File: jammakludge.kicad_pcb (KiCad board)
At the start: 2 copper layers, 55 parts, among them J1 Conn_02x28_Odd_Even, J2 Conn_02x28, J3 Conn_02x28

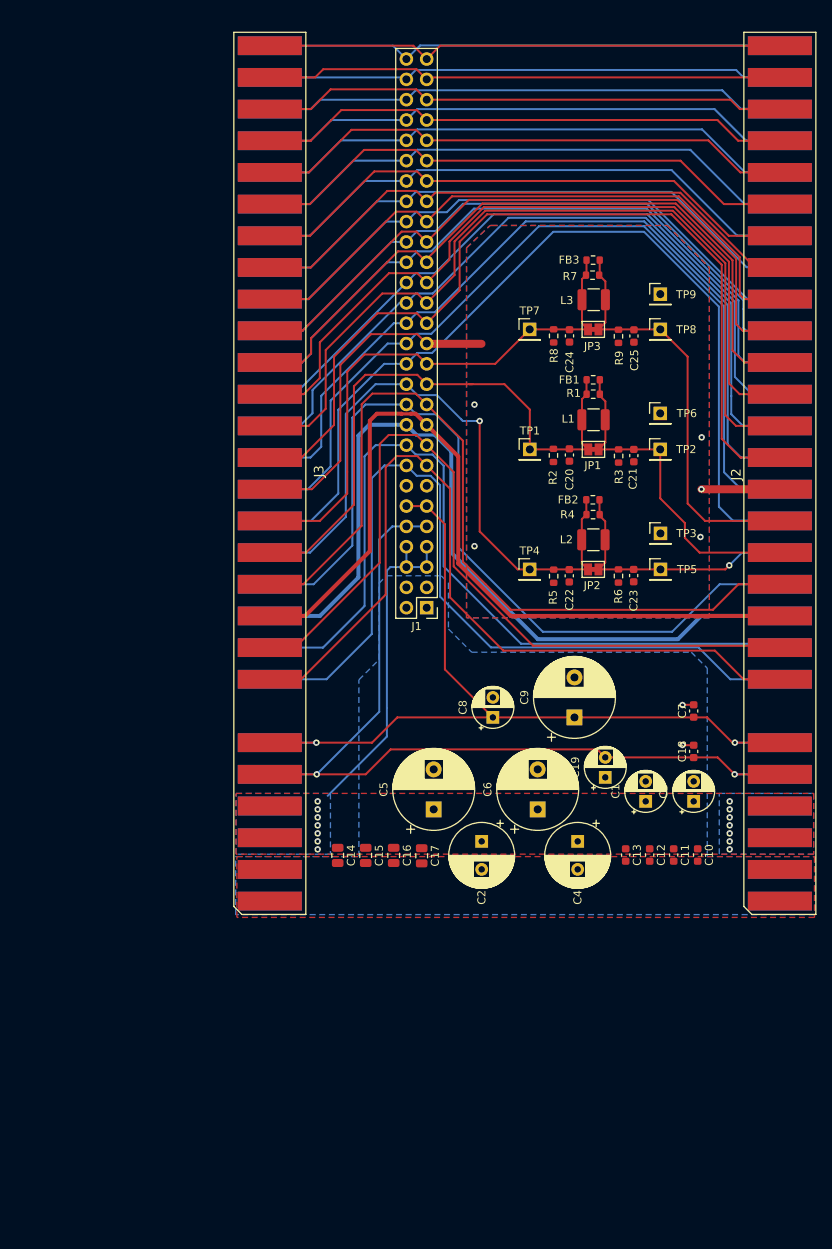
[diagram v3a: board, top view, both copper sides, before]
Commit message: Layout is basically complete, missing outline until dimensions can be double checked. DRC violations minimised but footprints (solder jumper and jamma edge connector) cause violations.
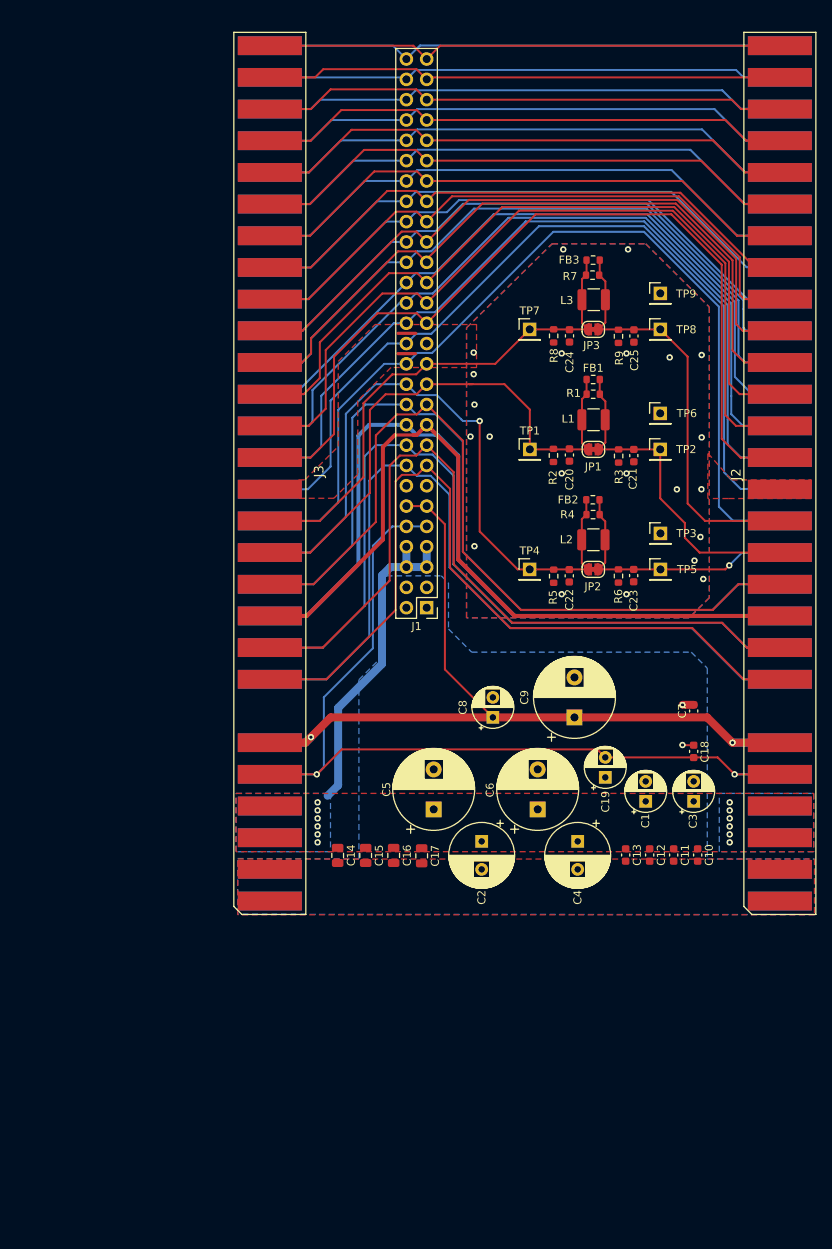
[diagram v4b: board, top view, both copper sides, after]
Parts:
- JP1, JP2, JP3: footprint Jumper:SolderJumper-2_P1.3mm_Bridged_Pad1.0x1.5mm -> Jumper:SolderJumper-2_P1.3mm_Bridged_RoundedPad1.0x1.5mm
- moved TP9 0.09 mm to (100.8, 79.0)
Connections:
- FB1 pad 1: (no net) -> /VidRedIn
- FB1 pad 2: (no net) -> /VidRed
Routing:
- net /VidGnd: track 52.3 -> 4.55 mm, vias 5 -> 22
- net /VidBlueIn: track 72.3 -> 67.9 mm
- net /Audio_+: track 103.9 -> 99.5 mm
- net /Speaker_+: track 102.1 -> 97.9 mm
- net /VidRedIn: track 74.0 -> 70.4 mm
- net /Speaker_-: track 103.7 -> 100.6 mm
- net /Meter_1: track 104.2 -> 101.1 mm
- net /Test_switch: track 111.3 -> 108.4 mm
- net /Meter_2: track 105.5 -> 102.6 mm
- net /Coin_1: track 104.9 -> 102.4 mm
- net /Audio_gnd: track 104.7 -> 102.5 mm
- net /Lockout_1: track 101.4 -> 99.9 mm
- net /P1_start: track 97.0 -> 95.6 mm
- net /Lockout_2: track 103.0 -> 102.2 mm
- net /VidSync: track 114.5 -> 115.1 mm
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
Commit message: added outline
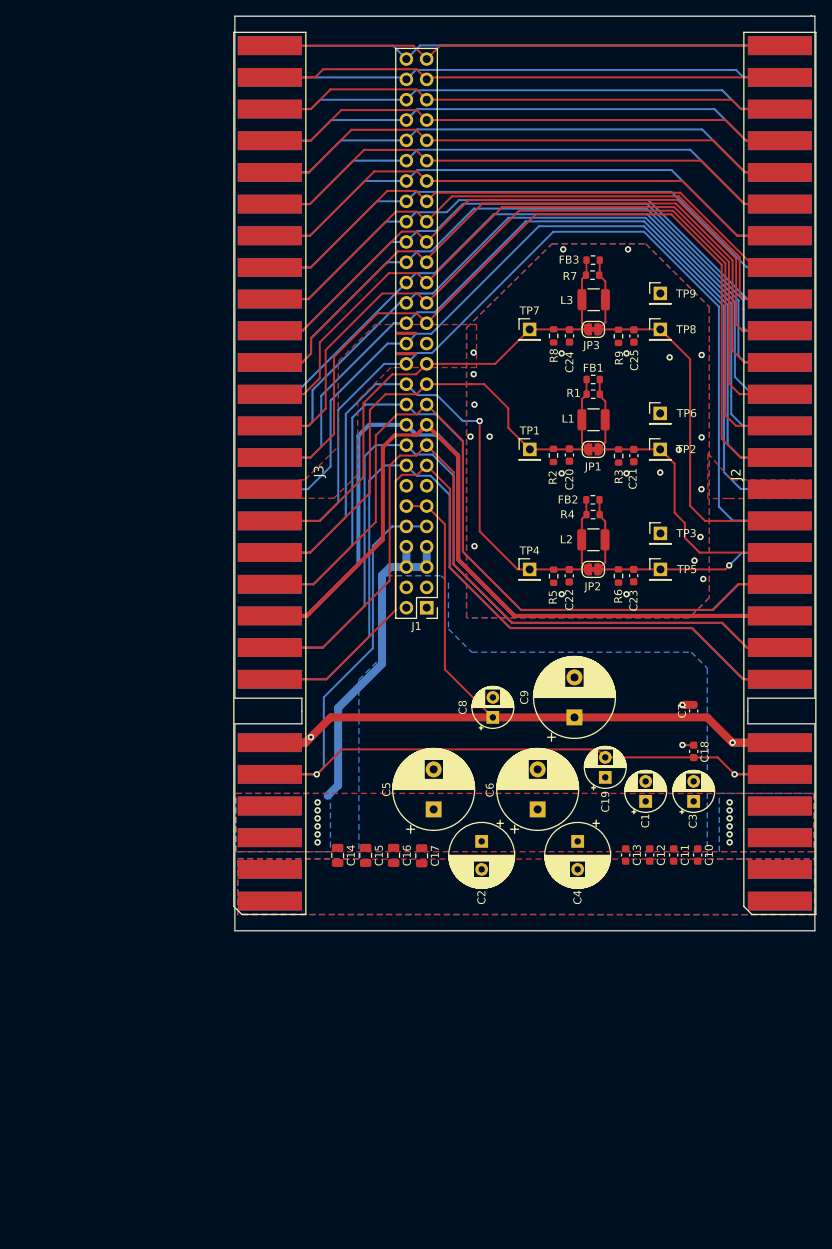
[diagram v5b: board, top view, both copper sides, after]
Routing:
- net /VidRedIn: track 70.4 -> 68.9 mm
- net /VidGnd: vias 22 -> 23
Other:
- board outline added: 72.5 x 114.3 mm
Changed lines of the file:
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@@
     )
   )
-  (segment (start 84.5196 93.5196) (end 81.3478 90.3478) (width 0.25) (layer "F.Cu") (net 1))
+  (gr_line (start 119.78 44.35) (end 119.6 44.35) (layer "Edge.Cuts") (width 0.05))
+  (gr_line (start 120.15 158.67) (end 47.65 158.67) (layer "Edge.Cuts") (width 0.05))
+  (gr_line (start 111.77 131.2) (end 111.77 129.6) (layer "Edge.Cuts") (width 0.05))
+  (gr_line (start 111.77 132.8) (end 120.15 132.8) (layer "Edge.Cuts") (width 0.05))
+  (gr_line (start 56.03 129.6) (end 47.65 129.6) (layer "Edge.Cuts") (width 0.05))
+  (gr_line (start 56.03 129.6) (end 56.03 131.2) (layer "Edge.Cuts") (width 0.05))
+  (gr_line (start 56.03 131.2) (end 56.03 132.8) (layer "Edge.Cuts") (width 0.05))
+  (gr_line (start 47.65 44.35) (end 120.15 44.35) (layer "Edge.Cuts") (width 0.05))
+  (gr_line (start 47.65 129.6) (end 47.65 44.35) (layer "Edge.Cuts") (width 0.05))
+  (gr_line (start 47.65 158.67) (end 47.65 132.8) (layer "Edge.Cuts") (width 0.05))
+  (gr_line (start 120.15 132.8) (end 120.15 158.67) (layer "Edge.Cuts") (width 0.05))
+  (gr_line (start 111.77 129.6) (end 120.15 129.6) (layer "Edge.Cuts") (width 0.05))
+  (gr_line (start 56.03 132.8) (end 47.65 132.8) (layer "Edge.Cuts") (width 0.05))
+  (gr_line (start 120.15 44.35) (end 120.15 129.6) (layer "Edge.Cuts") (width 0.05))
+  (gr_line (start 111.77 132.8) (end 111.77 131.2) (layer "Edge.Cuts") (width 0.05))
   (segment (start 52.0192 111.3972) (end 57.0728 111.3972) (width 0.25) (layer "F.Cu") (net 1))
   (segment (start 66.48 91.61) (end 70.3658 91.61) (width 0.25) (layer "F.Cu") (net 1))
@@
   (segment (start 57.0728 111.3972) (end 64.53 103.94) (width 0.25) (layer "F.Cu") (net 1))
   (segment (start 77.3478 90.3478) (end 76.9478 90.3478) (width 0.25) (layer "F.Cu") (net 1))
+  (segment (start 78.8078 90.3478) (end 76.9478 90.3478) (width 0.25) (layer "F.Cu") (net 1))
   (segment (start 91.6044 89.8386) (end 91.6044 91.6524) (width 0.25) (layer "F.Cu") (net 1))
   (segment (start 91.0385 94.7916) (end 91.0385 92.2183) (width 0.25) (layer "F.Cu") (net 1))
   (segment (start 91.0385 97.7383) (end 91.0385 94.7916) (width 0.25) (layer "F.Cu") (net 1))
   (segment (start 91.0385 92.2183) (end 91.5386 91.7182) (width 0.25) (layer "F.Cu") (net 1))
+  (segment (start 84.5196 98.5) (end 81.83 95.8104) (width 0.25) (layer "F.Cu") (net 1))
   (segment (start 64.53 93.56) (end 66.48 91.61) (width 0.25) (layer "F.Cu") (net 1))
   (segment (start 64.53 103.94) (end 64.53 93.56) (width 0.25) (layer "F.Cu") (net 1))
   (segment (start 76.9478 90.3478) (end 71.628 90.3478) (width 0.25) (layer "F.Cu") (net 1))
   (segment (start 91.8002 98.5) (end 91.0385 97.7383) (width 0.25) (layer "F.Cu") (net 1))
-  (segment (start 81.3478 90.3478) (end 76.9478 90.3478) (width 0.25) (layer "F.Cu") (net 1))
-  (segment (start 84.5196 98.5) (end 84.5196 93.5196) (width 0.25) (layer "F.Cu") (net 1))
+  (segment (start 81.83 95.8104) (end 81.83 93.37) (width 0.25) (layer "F.Cu") (net 1))
   (segment (start 70.3658 91.61) (end 71.628 90.3478) (width 0.25) (layer "F.Cu") (net 1))
+  (segment (start 81.83 93.37) (end 78.8078 90.3478) (width 0.25) (layer "F.Cu") (net 1))
+  (segment (start 102.61 100.2904) (end 100.8196 98.5) (width 0.25) (layer "F.Cu") (net 2))
   (segment (start 93.1002 98.5) (end 93.9635 97.6367) (width 0.25) (layer "F.Cu") (net 2))
-  (segment (start 103.9 109.55) (end 103.9 107.7) (width 0.25) (layer "F.Cu") (net 2))
   (segment (start 93.1002 98.5) (end 100.8322 98.5) (width 0.25) (layer "F.Cu") (net 2))
-  (segment (start 100.8196 104.6196) (end 100.8196 98.5) (width 0.25) (layer "F.Cu") (net 2))
-  (segment (start 103.9 107.7) (end 100.8196 104.6196) (width 0.25) (layer "F.Cu") (net 2))
+  (segment (start 102.61 106.41) (end 102.61 100.2904) (width 0.25) (layer "F.Cu") (net 2))
+  (segment (start 103.9 107.7) (end 102.61 106.41) (width 0.25) (layer "F.Cu") (net 2))
+  (segment (start 105.7472 111.3972) (end 103.9 109.55) (width 0.25) (layer "F.Cu") (net 2))
   (segment (start 93.2544 89.8386) (end 93.2544 91.6524) (width 0.25) (layer "F.Cu") (net 2))
   (segment (start 93.9635 94.7916) (end 93.9635 92.4931) (width 0.25) (layer "F.Cu") (net 2))
-  (segment (start 105.7472 111.3972) (end 115.7732 111.3972) (width 0.25) (layer "F.Cu") (net 2))
   (segment (start 93.9635 92.4931) (end 93.1886 91.7182) (width 0.25) (layer "F.Cu") (net 2))
-  (segment (start 105.7472 111.3972) (end 103.9 109.55) (width 0.25) (layer "F.Cu") (net 2))
+  (segment (start 103.9 109.55) (end 103.9 107.7) (width 0.25) (layer "F.Cu") (net 2))
+  (segment (start 115.7732 111.3972) (end 105.7472 111.3972) (width 0.25) (layer "F.Cu") (net 2))
   (segment (start 93.9635 97.6367) (end 93.9635 94.7916) (width 0.25) (layer "F.Cu") (net 2))
   (segment (start 84.5 113.5) (end 83 113.5) (width 0.25) (layer "F.Cu") (net 3))
@@
   (segment (start 63.72 92.73) (end 67.33 89.12) (width 0.25) (layer "F.Cu") (net 5))
   (segment (start 93.9635 77.4931) (end 93.1886 76.7182) (width 0.25) (layer "F.Cu") (net 6))
-  (segment (start 104.2416 105.2576) (end 104.2416 86.9094) (width 0.25) (layer "F.Cu") (net 6))
   (segment (start 93.9635 82.6367) (end 93.9635 79.7916) (width 0.25) (layer "F.Cu") (net 6))
+  (segment (start 106.4212 107.4372) (end 104.56 105.576) (width 0.25) (layer "F.Cu") (net 6))
   (segment (start 93.1002 83.5) (end 100.8322 83.5) (width 0.25) (layer "F.Cu") (net 6))
-  (segment (start 104.2416 105.2576) (end 106.4212 107.4372) (width 0.25) (layer "F.Cu") (net 6))
+  (segment (start 104.56 105.576) (end 104.56 87.2278) (width 0.25) (layer "F.Cu") (net 6))
   (segment (start 93.1002 83.5) (end 93.9635 82.6367) (width 0.25) (layer "F.Cu") (net 6))
+  (segment (start 104.56 87.2278) (end 100.8322 83.5) (width 0.25) (layer "F.Cu") (net 6))
   (segment (start 93.2544 74.8386) (end 93.2544 76.6524) (width 0.25) (layer "F.Cu") (net 6))
   (segment (start 93.9635 79.7916) (end 93.9635 77.4931) (width 0.25) (layer "F.Cu") (net 6))
-  (segment (start 106.4212 107.4372) (end 115.7732 107.4372) (width 0.25) (layer "F.Cu") (net 6))
   (segment (start 93.2544 76.6524) (end 93.1886 76.7182) (width 0.25) (layer "F.Cu") (net 6))
-  (segment (start 104.2416 86.9094) (end 100.8322 83.5) (width 0.25) (layer "F.Cu") (net 6))
+  (segment (start 115.7732 107.4372) (end 106.4212 107.4372) (width 0.25) (layer "F.Cu") (net 6))
   (segment (start 105 130.425) (end 103.625 130.425) (width 1) (layer "F.Cu") (net 7))
   (segment (start 105 135.475) (end 103.625 135.475) (width 0.25) (layer "F.Cu") (net 7))
@@
   (via (at 96.6 86.5) (size 0.8) (drill 0.4) (layers "F.Cu" "B.Cu") (net 51))
   (via (at 77.6 92.9) (size 0.8) (drill 0.4) (layers "F.Cu" "B.Cu") (net 51))
-  (via (at 102.9 103.5) (size 0.8) (drill 0.4) (layers "F.Cu" "B.Cu") (net 51))
+  (via (at 103.15 98.55) (size 0.8) (drill 0.4) (layers "F.Cu" "B.Cu") (net 51))
   (via (at 88.5 86.5) (size 0.8) (drill 0.4) (layers "F.Cu" "B.Cu") (net 51))
   (via (at 77.1 96.9) (size 0.8) (drill 0.4) (layers "F.Cu" "B.Cu") (net 51))
@@
   (via (at 77.6 110.6) (size 0.8) (drill 0.4) (layers "F.Cu" "B.Cu") (net 51))
   (via (at 77.5 89.1) (size 0.8) (drill 0.4) (layers "F.Cu" "B.Cu") (net 51))
+  (via (at 100.82 101.39) (size 0.8) (drill 0.4) (layers "F.Cu" "B.Cu") (net 51))
   (via (at 88.7 73.5) (size 0.8) (drill 0.4) (layers "F.Cu" "B.Cu") (net 51))
   (via (at 96.8 73.5) (size 0.8) (drill 0.4) (layers "F.Cu" "B.Cu") (net 51))
